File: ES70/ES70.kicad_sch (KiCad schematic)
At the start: 1 part

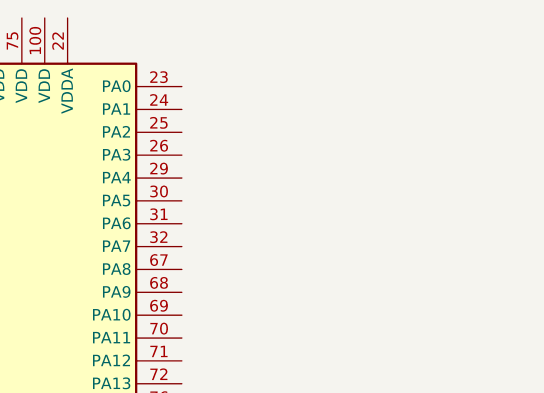
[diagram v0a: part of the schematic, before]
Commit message: Duplex Matrix schematic created, needs LED wiring still
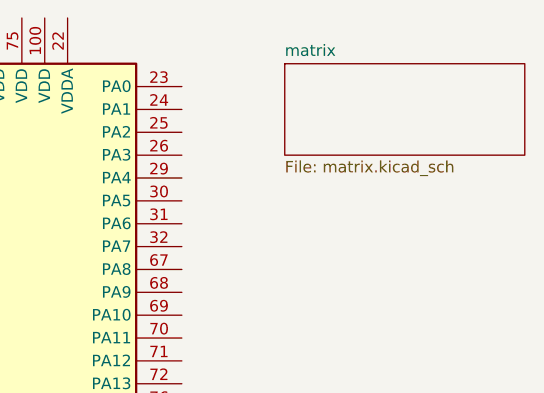
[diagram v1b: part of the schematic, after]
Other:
- added sheet matrix (matrix.kicad_sch)
